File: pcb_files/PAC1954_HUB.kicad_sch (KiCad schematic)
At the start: 11 parts, among them U26 PAC1954T-E_4MX

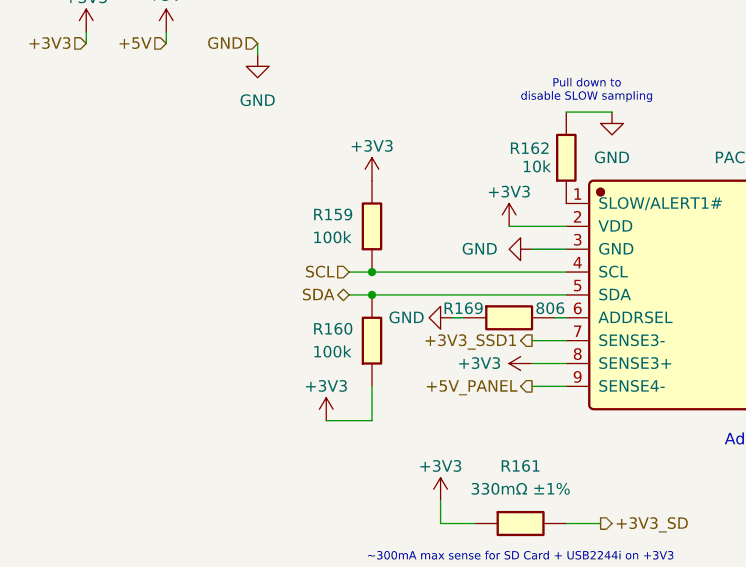
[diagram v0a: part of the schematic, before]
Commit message: Basic Function Review/Documentation for MCP9808
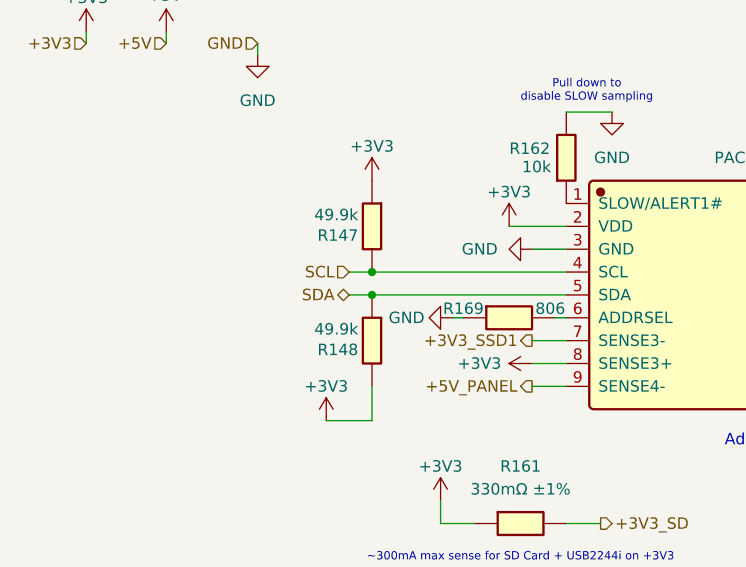
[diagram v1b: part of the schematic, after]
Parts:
- removed R159, R160: 100k, Resistor_SMD:R_0402_1005Metric, symbol JLCImport:0402WGF1003TCE
- added R147, R148: 49.9k, Resistor_SMD:R_0402_1005Metric, symbol JLCImport:RMS04FT4992
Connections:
- net +3V3: now also R147.1, R148.2
- net SCL: now also R147.2
- net SDA: now also R148.1

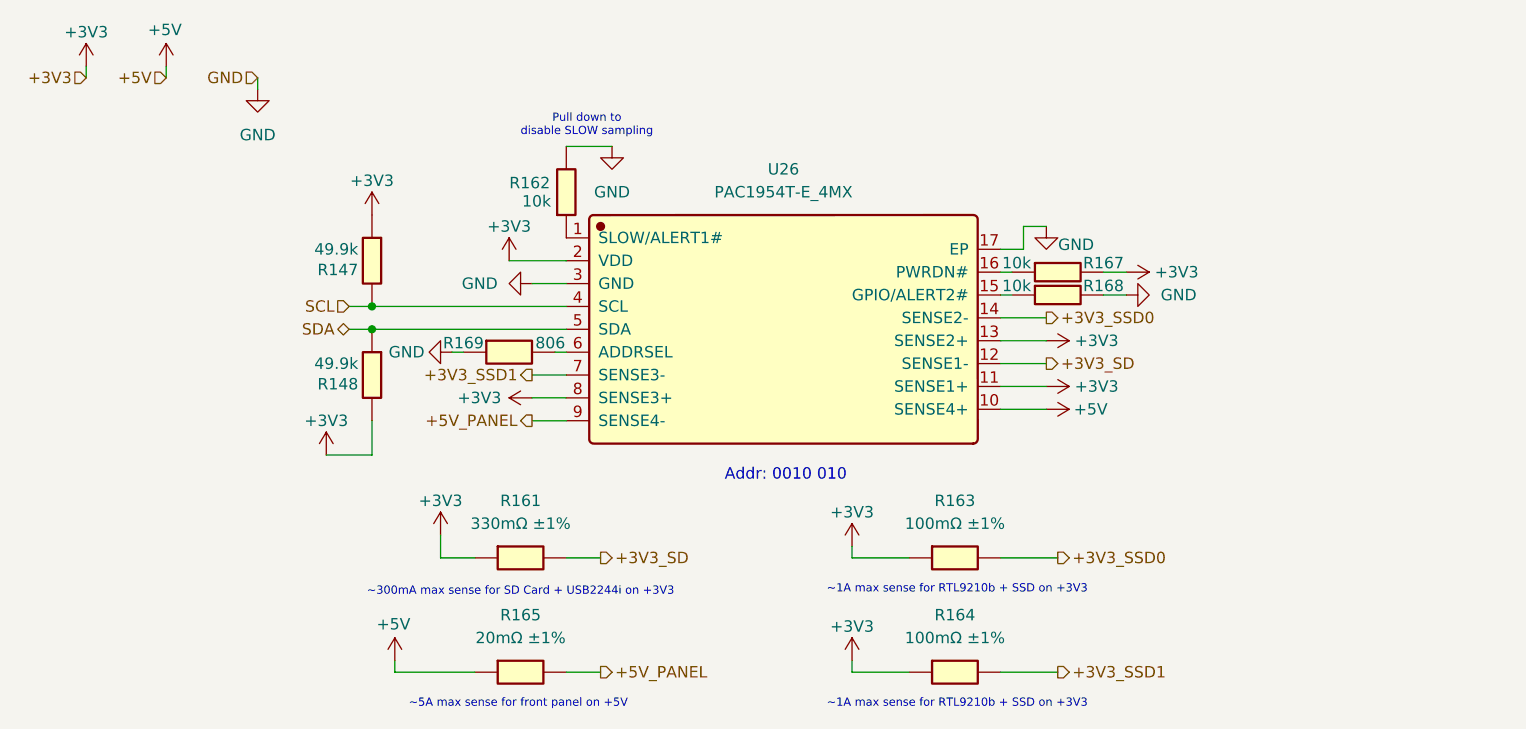
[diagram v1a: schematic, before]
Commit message: Switched PAC1954 to SLOW mode to save power
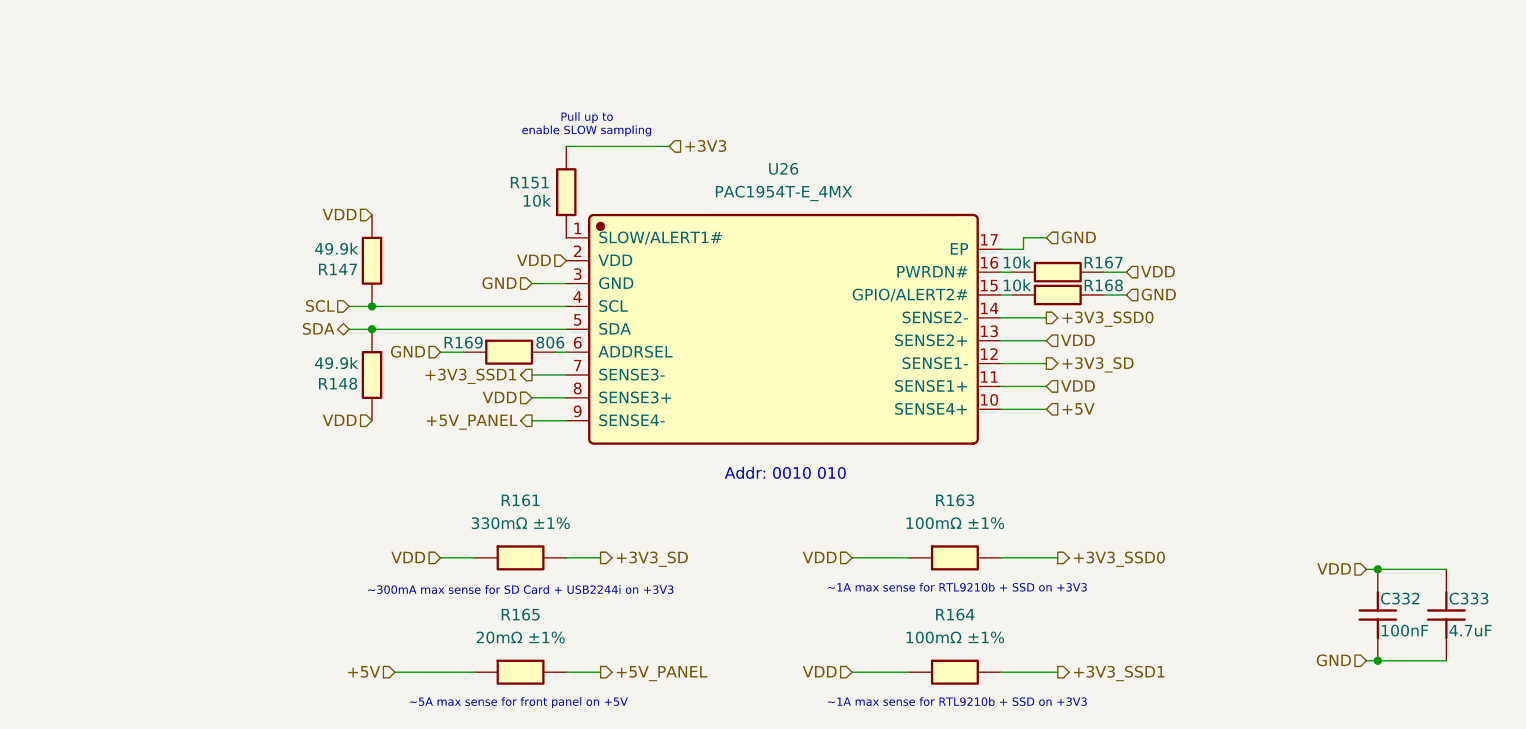
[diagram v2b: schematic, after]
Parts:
- removed R162: 10k, Resistor_SMD:R_0402_1005Metric, symbol JLCImport:0402WGF1002TCE
- added C332: 100nF, Capacitor_SMD:C_0402_1005Metric, symbol JLCImport:CL05B104KB54PNC
- added C333: 4.7uF, Capacitor_SMD:C_0402_1005Metric, symbol JLCImport:CL05A475MP5NRNC
- added R151: 10k, Resistor_SMD:R_0402_1005Metric, symbol JLCImport:0402WGF1002TCE
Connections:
- net +3V3: now also R151.2; no longer R147.1, R148.2, R161.1, R163.1, R164.1, R167.2, U26.11 (SENSE1+), U26.13 (SENSE2+), U26.2 (VDD), U26.8 (SENSE3+)
- net GND: now also C332.1, C333.1
- net at U26.1 (SLOW/ALERT1#): now also R151.1
- new net VDD: C332.2, C333.2, R147.1, R148.2, R161.1, R163.1, R164.1, R167.2, U26.11 (SENSE1+), U26.13 (SENSE2+), U26.2 (VDD), U26.8 (SENSE3+)
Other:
- note added: "Pull up to enable SLOW sampling"
- note removed: "Pull down to disable SLOW sampling"

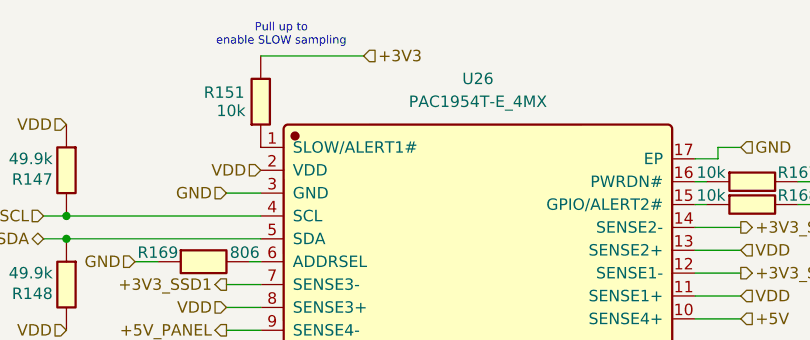
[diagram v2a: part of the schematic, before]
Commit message: Added FAN4 and updated RP2354/PAC1954 to match
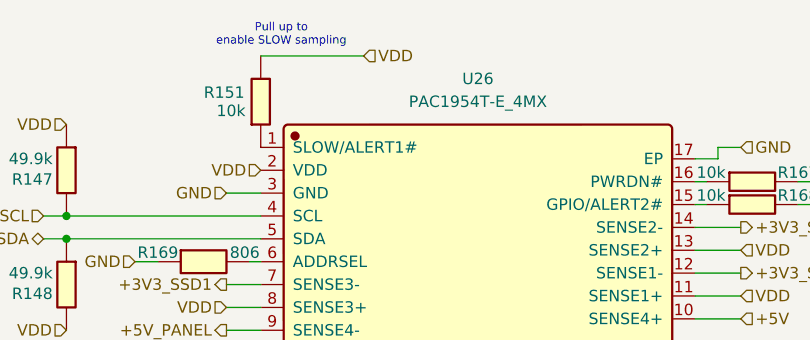
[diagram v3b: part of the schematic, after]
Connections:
- net +3V3 is gone; now on net VDD: R151.2
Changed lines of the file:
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@@
+	(hierarchical_label "VDD"
+		(shape input)
+		(at 90.17 30.48 0)
+		(effects
+			(font
+				(size 1.27 1.27)
+			)
+			(justify left)
+		)
+	)
 	(hierarchical_label "VDD"
 		(shape input)
@@
 		(effects
 			(font
-				(size 1.27 1.27)
-			)
-			(justify left)
-		)
-	)
-	(hierarchical_label "+3V3"
-		(shape input)
-		(at 90.17 30.48 0)
-		(effects
-			(font
